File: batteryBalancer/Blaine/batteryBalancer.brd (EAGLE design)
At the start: 101.6 x 101.6 mm, 30 parts

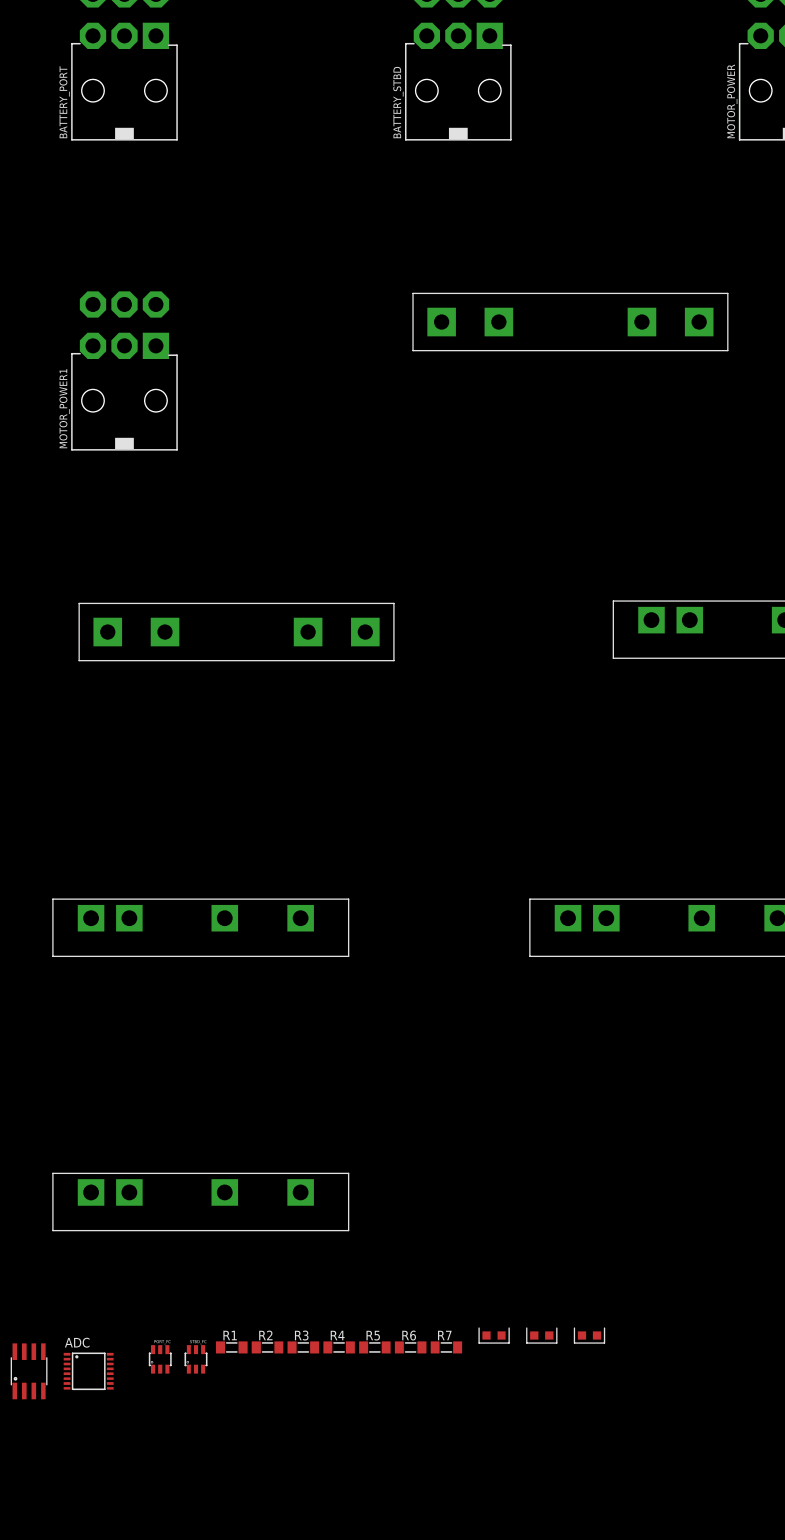
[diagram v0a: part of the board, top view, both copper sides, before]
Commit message: Fancied up the schematic, nets still need to be named
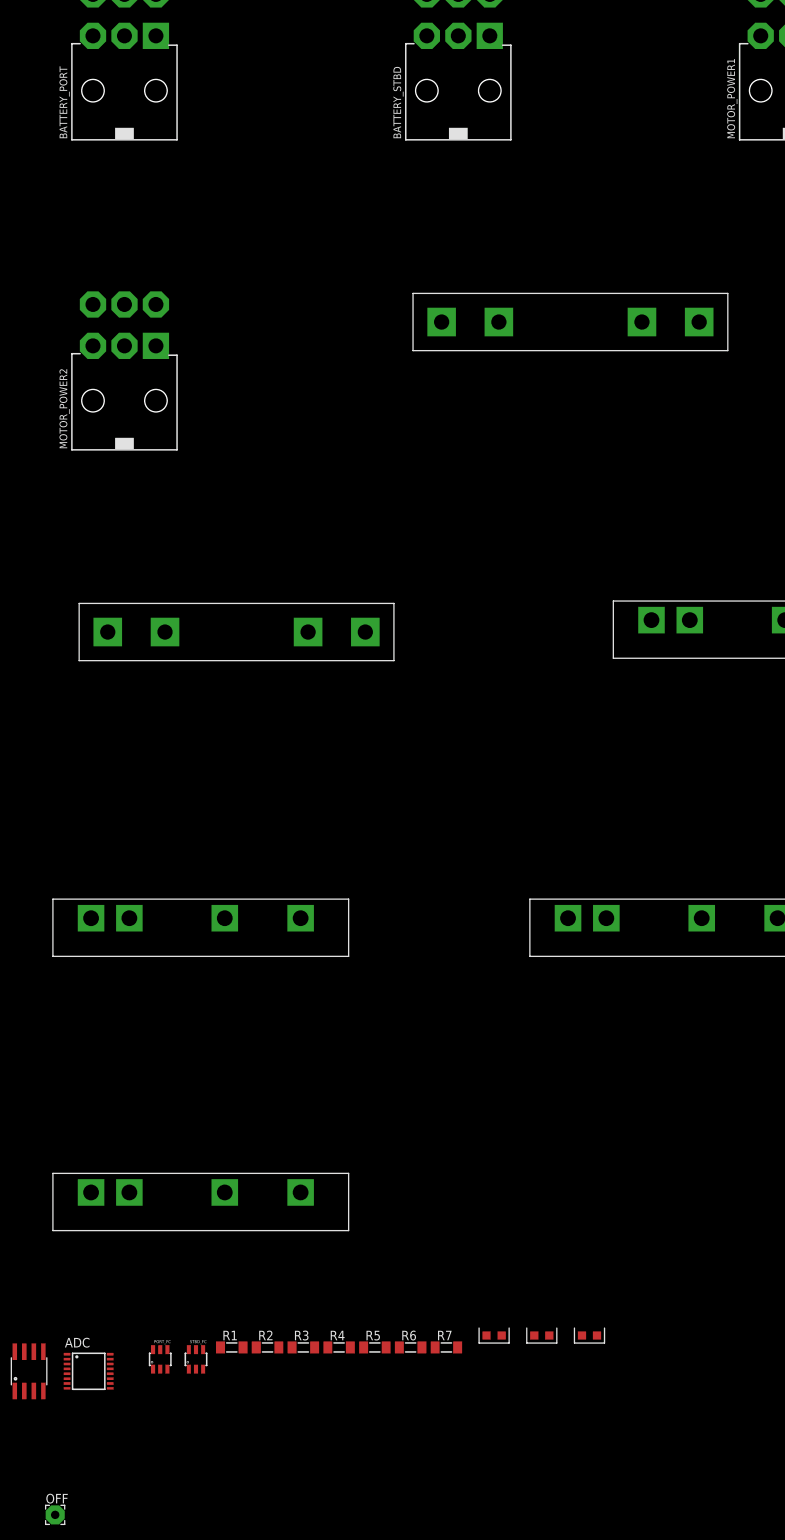
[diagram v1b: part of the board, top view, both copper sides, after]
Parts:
- removed MOTOR_POWER: 39-30-06?, con-molex-mini-fit:39-30-?06?
- added MOTOR_POWER2: 39-30-06?, con-molex-mini-fit:39-30-?06?
- added OFF: (no value), wirepad:2,54/1,1
- moved MOTOR_POWER1 98.0 mm to (111.1, -65.1)
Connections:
- removed net N$10 (its old number): EDGE_CONNECTOR.GND1, EDGE_CONNECTOR.GND2, EDGE_CONNECTOR.GND3, RELAY2.CONTROL-, RELAY3.CONTROL-, RELAY4.CONTROL-, RLAY1.CONTROL-
- new net N$15: OFF.1, PORT_FC.3, STBD_FC.3
- net GND: now also MOTOR_POWER2.4, MOTOR_POWER2.5, MOTOR_POWER2.6; no longer MOTOR_POWER.4, MOTOR_POWER.5, MOTOR_POWER.6
- net LOGIC_GND: now also EDGE_CONNECTOR.GND1, EDGE_CONNECTOR.GND2, EDGE_CONNECTOR.GND3, RELAY2.CONTROL-, RELAY3.CONTROL-, RELAY4.CONTROL-, RLAY1.CONTROL-
- net N$22: now also MOTOR_POWER2.1, MOTOR_POWER2.2, MOTOR_POWER2.3; no longer MOTOR_POWER1.1, MOTOR_POWER1.2, MOTOR_POWER1.3
- net N$5: now also MOTOR_POWER1.1, MOTOR_POWER1.2, MOTOR_POWER1.3; no longer MOTOR_POWER.1, MOTOR_POWER.2, MOTOR_POWER.3
